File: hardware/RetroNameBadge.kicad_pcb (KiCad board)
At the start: 4 copper layers, 83.8 x 52.1 mm, 49 parts, among them J1 Conn_8pin, Q1 MMBT3906, Q2 MMBT3906, U1 74HC595, U2 74HC595, U3 74HC595, U4 74HC595, U5 74HC595, U6 74HC595, U7 74HC595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

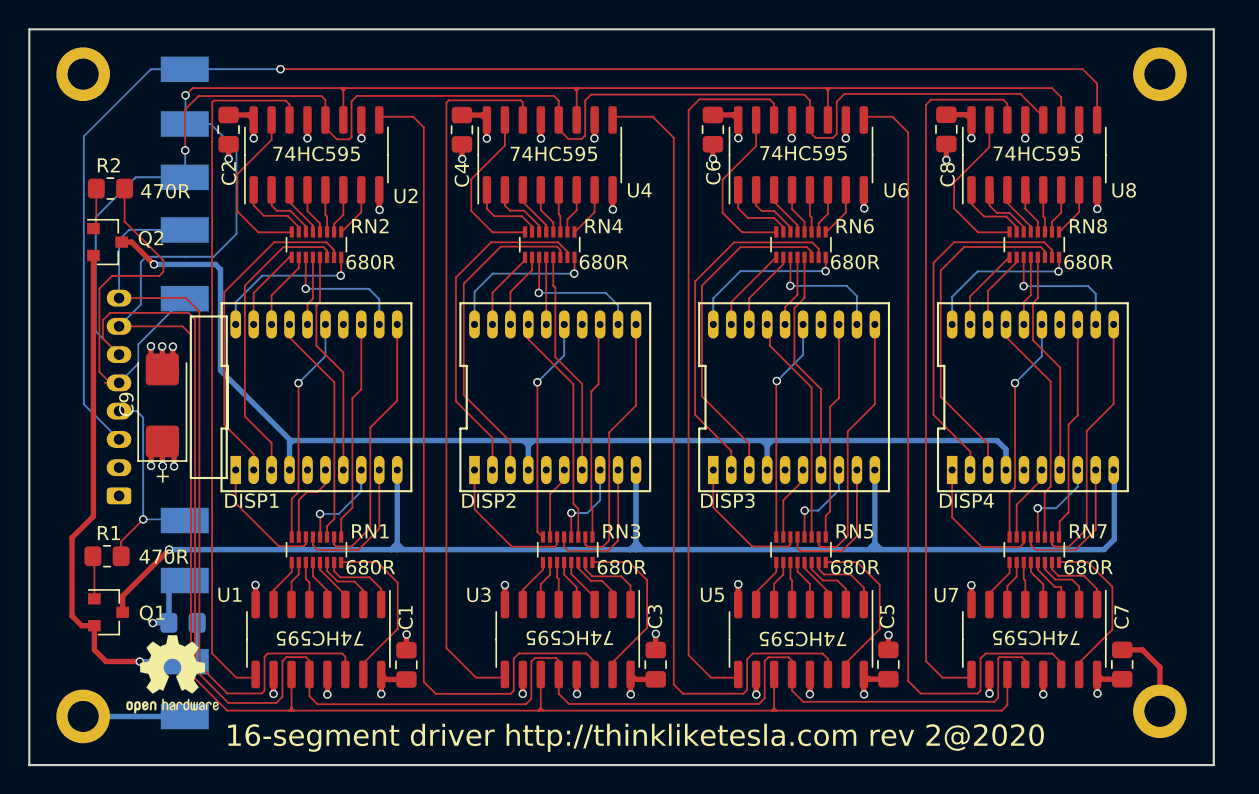
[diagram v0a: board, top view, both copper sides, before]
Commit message: Final rev2 sent to production
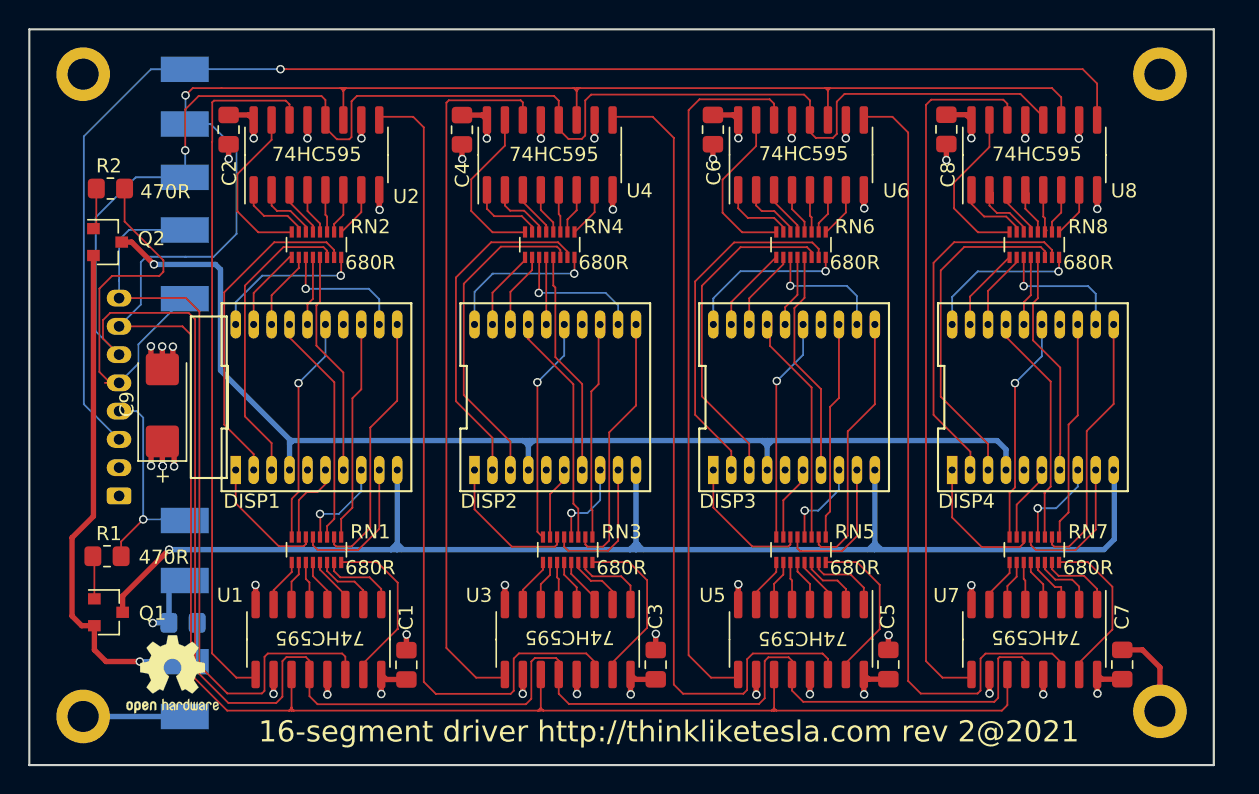
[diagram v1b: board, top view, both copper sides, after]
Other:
- board text added: "16-segment driver http://thinkliketesla.com rev 2@2021"
- board text removed: "16-segment driver http://thinkliketesla.com rev 2@2020"
